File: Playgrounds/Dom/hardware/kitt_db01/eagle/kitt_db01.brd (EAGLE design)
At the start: 50.8 x 31 mm, 13 parts, among them Q1 [MMBF170], U1 ADNS-3080, X1 RESON

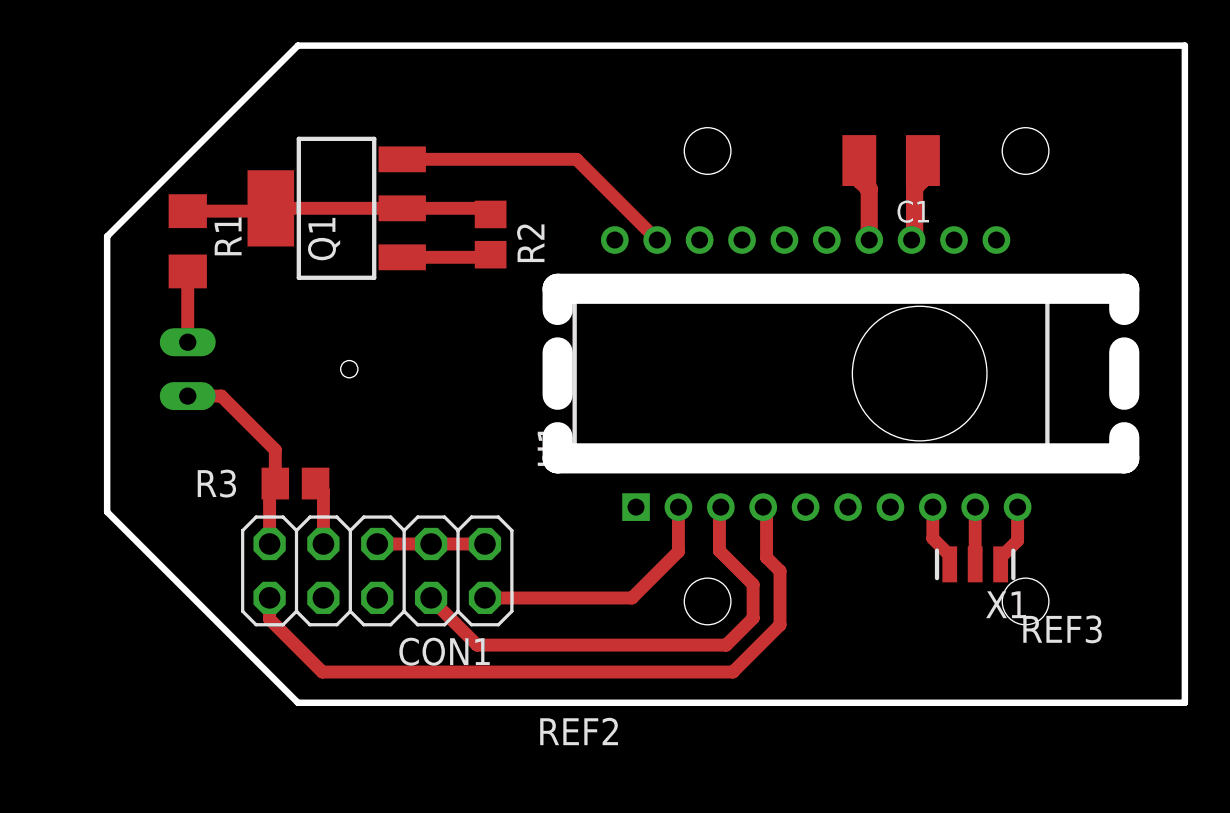
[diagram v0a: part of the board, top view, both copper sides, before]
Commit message: - added poly gnd pour  - cleaned up garbage files
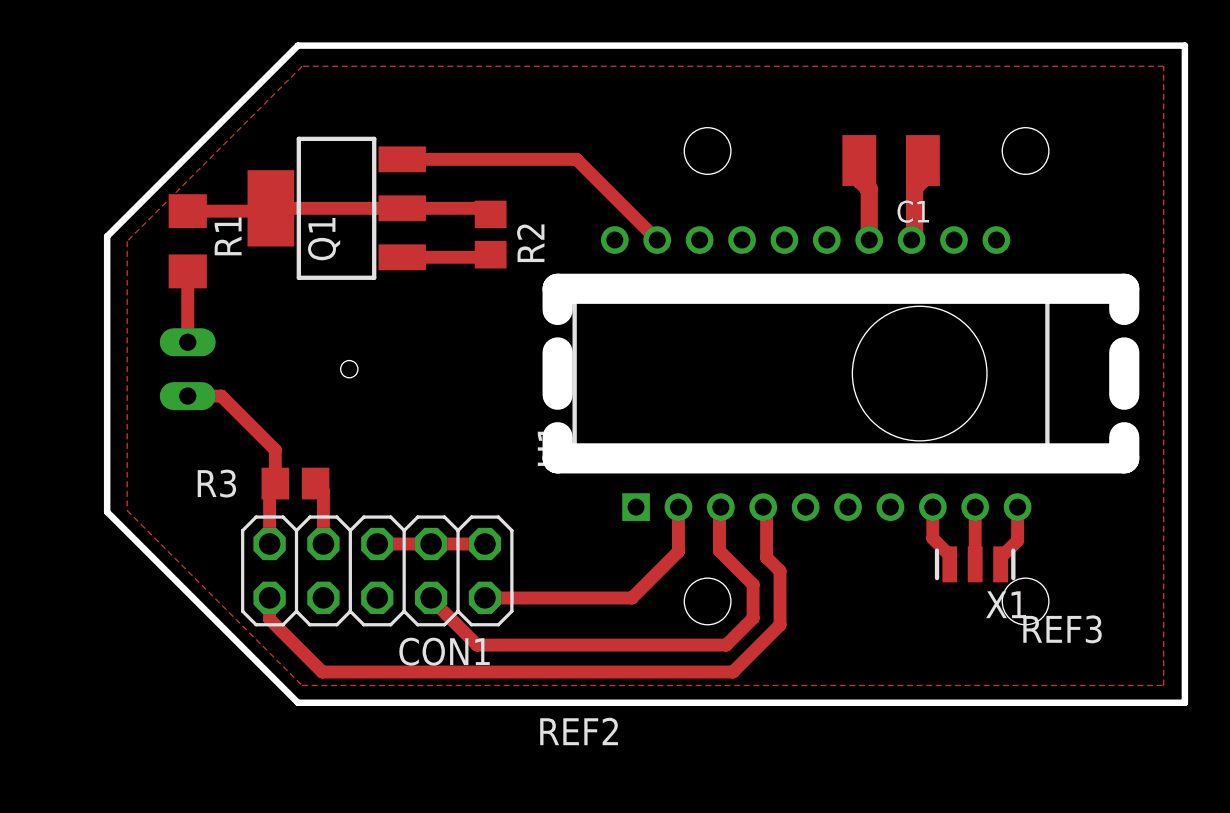
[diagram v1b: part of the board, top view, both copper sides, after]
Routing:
- added copper zone on layer 1, net GND
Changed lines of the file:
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@@
 <setting verticaltext="up"/>
 </settings>
-<grid distance="12.5" unitdist="mil" unit="mil" style="lines" multiple="1" display="yes" altdistance="0.0125" altunitdist="inch" altunit="inch"/>
+<grid distance="25" unitdist="mil" unit="mil" style="lines" multiple="1" display="yes" altdistance="0.0125" altunitdist="inch" altunit="inch"/>
 <layers>
 <layer number="1" name="Top" color="4" fill="1" visible="yes" active="yes"/>
@@
 <wire x1="79.7425" y1="50.49" x2="82.2825" y2="50.49" width="0.6096" layer="1"/>
 <wire x1="82.2825" y1="50.49" x2="84.8225" y2="50.49" width="0.6096" layer="1"/>
-<wire x1="92.949696875" y1="64.829321875" x2="98.949696875" y2="64.829321875" width="0" layer="19" extent="1-1"/>
-<wire x1="84.8225" y1="50.49" x2="92.949696875" y2="64.829321875" width="0" layer="19" extent="1-1"/>
 <wire x1="80.919" y1="68.636" x2="89.14301875" y2="68.636" width="0.6096" layer="1"/>
 <wire x1="89.14301875" y1="68.636" x2="92.949696875" y2="64.829321875" width="0.6096" layer="1"/>
+<polygon width="0.6096" layer="1" isolate="0.4064">
+<vertex x="67.945" y="52.07"/>
+<vertex x="76.2" y="43.815"/>
+<vertex x="116.84" y="43.815"/>
+<vertex x="116.84" y="73.025"/>
+<vertex x="76.2" y="73.025"/>
+<vertex x="67.945" y="64.77"/>
+</polygon>
 </signal>
 <signal name="N$1">
@@
 <contactref element="U1" pad="7"/>
 <contactref element="R3" pad="2"/>
-<wire x1="76.8325" y1="53.34" x2="103.949696875" y2="52.229321875" width="0" layer="19" extent="1-1"/>
 <wire x1="76.8325" y1="53.34" x2="77.2025" y2="52.97" width="0.6096" layer="1"/>
 <wire x1="77.2025" y1="52.97" x2="77.2025" y2="50.49" width="0.6096" layer="1"/>
+<wire x1="77.2025" y1="52.97" x2="103.949696875" y2="52.229321875" width="0" layer="19" extent="1-1"/>
 </signal>
 </signals>

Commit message: added keepout region around milling area
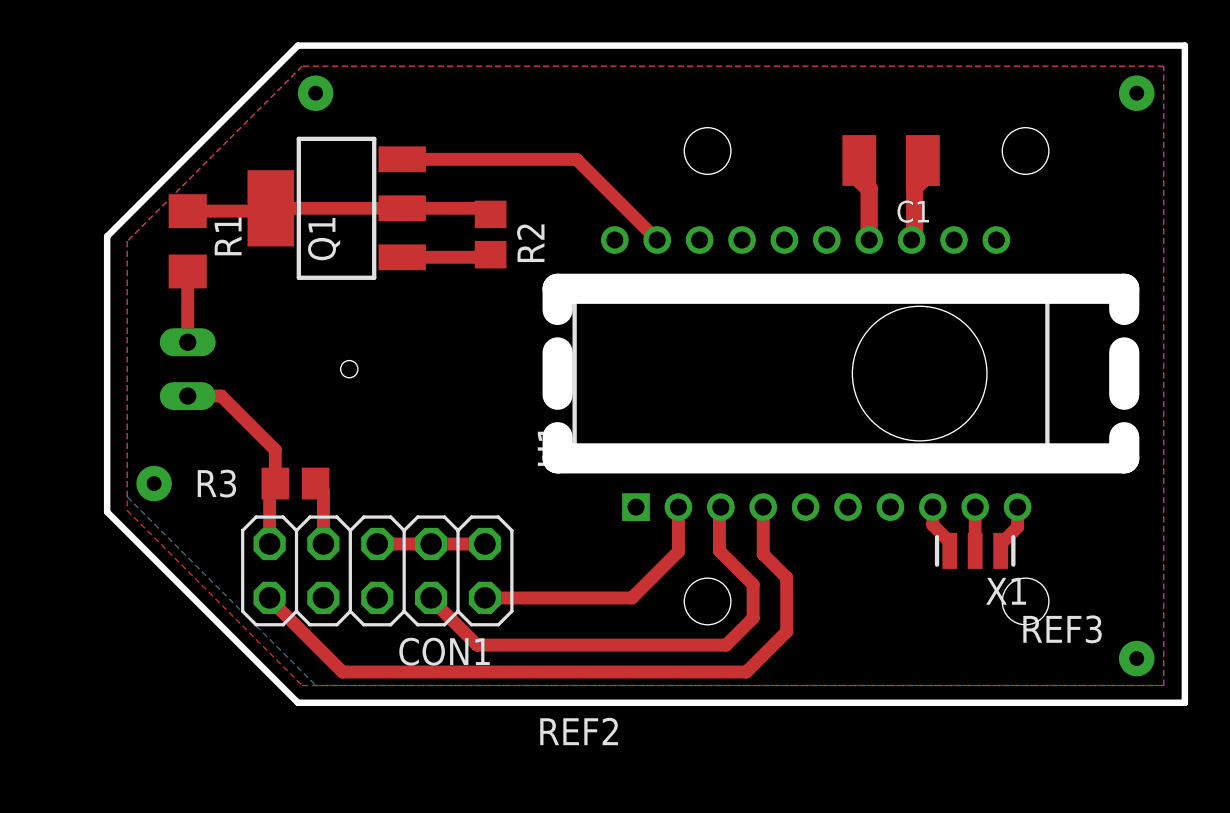
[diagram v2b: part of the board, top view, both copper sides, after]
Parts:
- moved X1 0.63 mm to (107.9, 50.2)
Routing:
- net N$3: track 3.03 -> 2.40 mm
- net N$2: track 3.03 -> 2.40 mm
- net N$1: track 2.70 -> 2.07 mm
- net GND: vias 0 -> 4
- added copper zone on layer 16, net GND
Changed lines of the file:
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@@
 <setting verticaltext="up"/>
 </settings>
-<grid distance="25" unitdist="mil" unit="mil" style="lines" multiple="1" display="yes" altdistance="0.0125" altunitdist="inch" altunit="inch"/>
+<grid distance="25" unitdist="mil" unit="mm" style="lines" multiple="1" display="yes" altdistance="0.0125" altunitdist="inch" altunit="inch"/>
 <layers>
 <layer number="1" name="Top" color="4" fill="1" visible="yes" active="yes"/>
@@
 <wire x1="76" y1="43" x2="117.84" y2="43" width="0.3048" layer="20"/>
 <wire x1="117.84" y1="43" x2="117.84" y2="74" width="0.3048" layer="20"/>
+<polygon width="0.6096" layer="41">
+<vertex x="87.63" y="63.5"/>
+<vertex x="87.63" y="53.34"/>
+<vertex x="116.205" y="53.34"/>
+<vertex x="116.205" y="63.5"/>
+</polygon>
+<polygon width="0.6096" layer="42">
+<vertex x="87.63" y="63.5"/>
+<vertex x="87.63" y="53.34"/>
+<vertex x="116.205" y="53.34"/>
+<vertex x="116.205" y="63.5"/>
+</polygon>
 </plain>
 <attributes>
@@
 <element name="REF3" library="scaleauto" package="SC-8000-C" value="SC-8000-C" x="126.575696875" y="58.529321875"/>
 <element name="U1" library="Ai_IC" package="ADNS-3080" value="ADNS-3080" x="100.075696875" y="58.529321875"/>
-<element name="X1" library="Ai_Passives" package="RESON-SMD" value="RESON" x="107.948696875" y="49.529321875" rot="R180"/>
+<element name="X1" library="Ai_Passives" package="RESON-SMD" value="RESON" x="107.948696875" y="50.164321875" rot="R180"/>
 <element name="U$1" library="frames" package="A3L-LOC" value="" x="-113.3475" y="-77.1525"/>
 <element name="CON1" library="pinhead" package="2X05" value="" x="79.7425" y="49.22" smashed="yes">
@@
 <vertex x="67.945" y="64.77"/>
 </polygon>
+<via x="69.215" y="53.34" extent="1-16" drill="0.7" diameter="1.6764"/>
+<polygon width="0.6096" layer="16" isolate="0.4064">
+<vertex x="67.945" y="64.77"/>
+<vertex x="67.945" y="52.705"/>
+<vertex x="76.835" y="43.815"/>
+<vertex x="116.84" y="43.815"/>
+<vertex x="116.84" y="73.025"/>
+<vertex x="76.2" y="73.025"/>
+</polygon>
+<via x="76.835" y="71.755" extent="1-16" drill="0.7" diameter="1.6764"/>
+<via x="115.57" y="71.755" extent="1-16" drill="0.7" diameter="1.6764"/>
+<via x="115.57" y="45.085" extent="1-16" drill="0.7" diameter="1.6764"/>
 </signal>
 <signal name="N$1">
 <contactref element="U1" pad="9"/>
 <contactref element="X1" pad="2"/>
-<wire x1="107.948696875" y1="49.529321875" x2="107.949696875" y2="49.530321875" width="0.6096" layer="1"/>
-<wire x1="107.949696875" y1="49.530321875" x2="107.949696875" y2="52.229321875" width="0.6096" layer="1"/>
+<wire x1="107.948696875" y1="50.164321875" x2="107.949696875" y2="50.165321875" width="0.6096" layer="1"/>
+<wire x1="107.949696875" y1="50.165321875" x2="107.949696875" y2="52.229321875" width="0.6096" layer="1"/>
 </signal>
 <signal name="N$2">
 <contactref element="X1" pad="3"/>
 <contactref element="U1" pad="8"/>
-<wire x1="105.949696875" y1="52.229321875" x2="105.949696875" y2="50.750521875" width="0.6096" layer="1"/>
-<wire x1="105.949696875" y1="50.750521875" x2="106.748696875" y2="49.951521875" width="0.6096" layer="1"/>
-<wire x1="106.748696875" y1="49.951521875" x2="106.748696875" y2="49.529321875" width="0.6096" layer="1"/>
+<wire x1="105.949696875" y1="52.229321875" x2="105.949696875" y2="51.385521875" width="0.6096" layer="1"/>
+<wire x1="105.949696875" y1="51.385521875" x2="106.748696875" y2="50.586521875" width="0.6096" layer="1"/>
+<wire x1="106.748696875" y1="50.586521875" x2="106.748696875" y2="50.164321875" width="0.6096" layer="1"/>
 </signal>
 <signal name="N$3">
 <contactref element="X1" pad="1"/>
 <contactref element="U1" pad="10"/>
-<wire x1="109.949696875" y1="52.229321875" x2="109.949696875" y2="50.648321875" width="0.6096" layer="1"/>
-<wire x1="109.949696875" y1="50.648321875" x2="109.148696875" y2="49.847321875" width="0.6096" layer="1"/>
-<wire x1="109.148696875" y1="49.847321875" x2="109.148696875" y2="49.529321875" width="0.6096" layer="1"/>
+<wire x1="109.949696875" y1="52.229321875" x2="109.949696875" y2="51.283321875" width="0.6096" layer="1"/>
+<wire x1="109.949696875" y1="51.283321875" x2="109.148696875" y2="50.482321875" width="0.6096" layer="1"/>
+<wire x1="109.148696875" y1="50.482321875" x2="109.148696875" y2="50.164321875" width="0.6096" layer="1"/>
 </signal>
 <signal name="+3V3">
@@
 <contactref element="CON1" pad="1"/>
 <contactref element="U1" pad="4"/>
-<wire x1="97.949696875" y1="52.229321875" x2="98.1075" y2="52.07151875" width="0.6096" layer="1"/>
-<wire x1="98.1075" y1="52.07151875" x2="98.1075" y2="49.8475" width="0.6096" layer="1"/>
-<wire x1="98.1075" y1="49.8475" x2="98.7425" y2="49.2125" width="0.6096" layer="1"/>
-<wire x1="98.7425" y1="49.2125" x2="98.7425" y2="46.6725" width="0.6096" layer="1"/>
-<wire x1="98.7425" y1="46.6725" x2="96.52" y2="44.45" width="0.6096" layer="1"/>
-<wire x1="96.52" y1="44.45" x2="77.1525" y2="44.45" width="0.6096" layer="1"/>
-<wire x1="77.1525" y1="44.45" x2="74.6625" y2="46.94" width="0.6096" layer="1"/>
-<wire x1="74.6625" y1="46.94" x2="74.6625" y2="47.95" width="0.6096" layer="1"/>
+<wire x1="74.6625" y1="47.95" x2="74.6625" y2="47.8925" width="0.6096" layer="1"/>
+<wire x1="74.6625" y1="47.8925" x2="78.105" y2="44.45" width="0.6096" layer="1"/>
+<wire x1="78.105" y1="44.45" x2="97.155" y2="44.45" width="0.6096" layer="1"/>
+<wire x1="97.155" y1="44.45" x2="99.06" y2="46.355" width="0.6096" layer="1"/>
+<wire x1="99.06" y1="46.355" x2="99.06" y2="48.895" width="0.6096" layer="1"/>
+<wire x1="99.06" y1="48.895" x2="97.949696875" y2="50.005303125" width="0.6096" layer="1"/>
+<wire x1="97.949696875" y1="50.005303125" x2="97.949696875" y2="52.229321875" width="0.6096" layer="1"/>
 </signal>
 <signal name="RST">

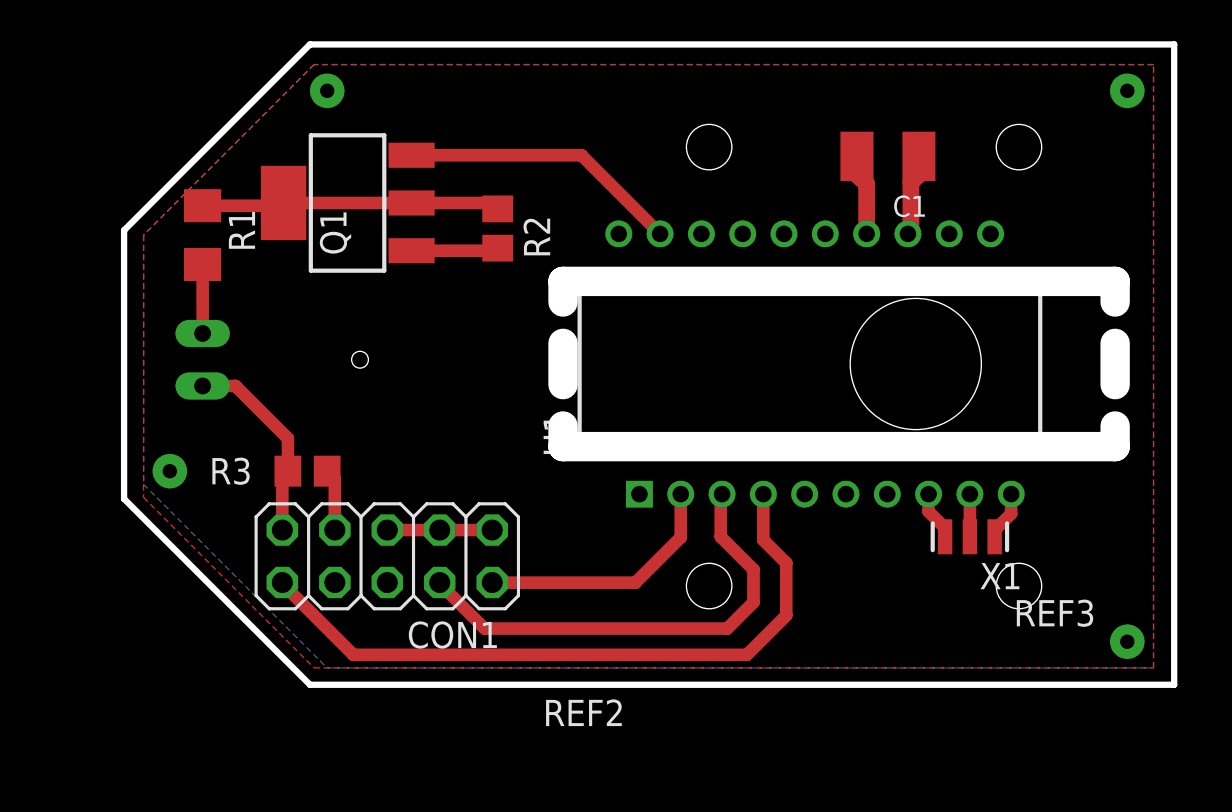
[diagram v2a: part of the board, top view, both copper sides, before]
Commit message: rough route and placement completed
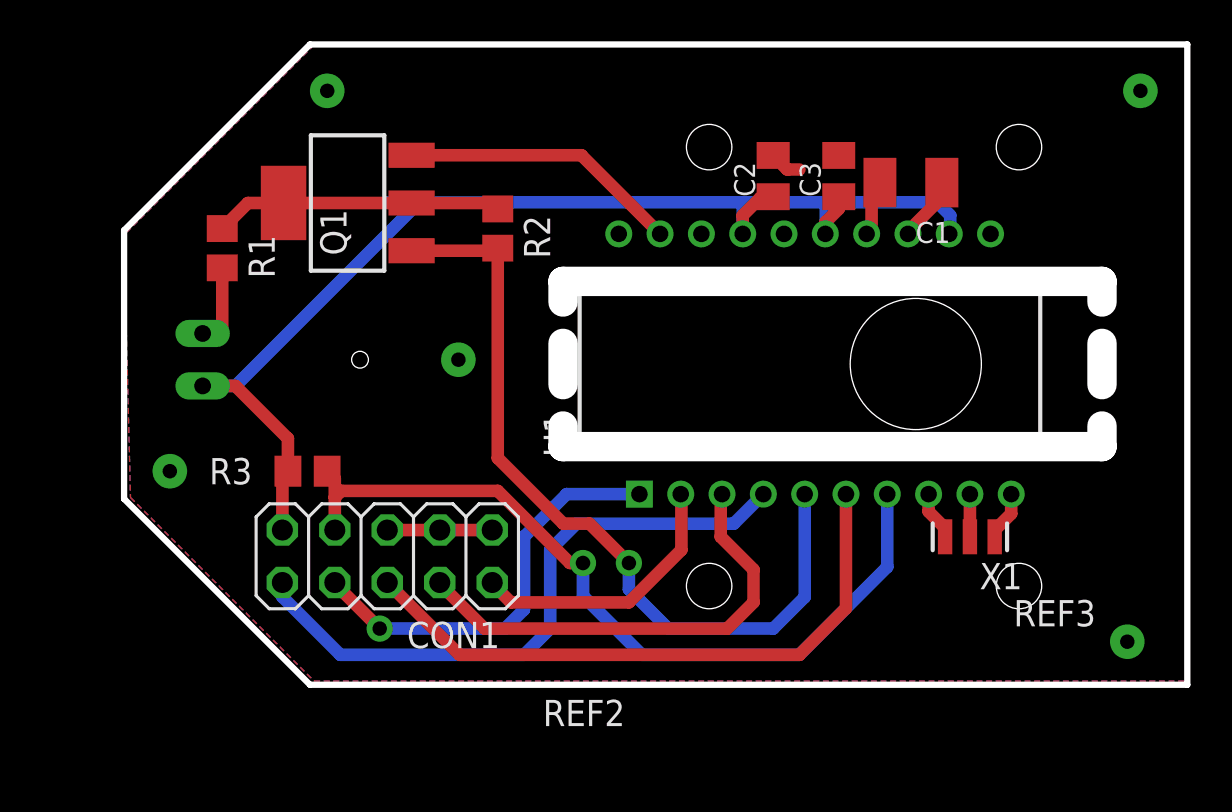
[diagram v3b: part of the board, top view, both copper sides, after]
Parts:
- added C2, C3: 100nF, rcl:C0805K
- R1: device rcl:R1206 -> rcl:R0805
- moved C1 1.69 mm to (105.1, 67.3)
- moved R1 1.14 mm to (71.8, 64.1)
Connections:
- net +3V3: now also C2.1, C3.1
- net GND: now also C2.2, C3.2
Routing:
- net +3V3: track 9.73 -> 60.3 mm
- net !PD: track 3.00 -> 39.4 mm, vias 0 -> 1
- net N$4: track 4.22 -> 39.0 mm, vias 0 -> 1
- net RST: track 0.00 -> 30.1 mm
- net !CS: track 0.00 -> 20.5 mm, vias 0 -> 1
- net MOSI: track 33.0 -> 30.8 mm
- net GND: track 18.7 -> 20.3 mm, vias 4 -> 5
- net MISO: track 12.1 -> 13.4 mm
- net N$6: track 3.94 -> 2.75 mm
- net N$5: track 3.97 -> 3.08 mm
- net N$8: track 3.34 -> 4.13 mm
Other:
- board size 50.8 x 31 mm -> 51.5 x 31 mm

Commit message: Board and Library Updates  - kitt.con.lbr: connectors and connector references    -> DB01 Odometry Board Connector + board outline    -> Arduino Uno shield pins + (pin) overlay for ghostcar  - kitt.ic.lbr: added battery charger component from prev. board
 - mb01.*: motherboard for scaleauto
   -> added board connectors
   -> extended board size and corrected mounting holes
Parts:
- added R4: [PPR], rcl:R0805
- moved R3 0.63 mm to (75.9, 54.0)
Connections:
- net !PD: now also R4.1
- net GND: now also R4.2
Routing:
- net !PD: track 39.4 -> 42.1 mm
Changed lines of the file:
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@@
 <element name="R2" library="rcl" package="R0805" value="[0R]" x="85.09" y="65.0875" rot="R270"/>
 <element name="R1" library="rcl" package="R0805" value="180R" x="71.755" y="64.135" rot="R270"/>
-<element name="R3" library="rcl" package="R0805" value="[PPR]" x="75.8825" y="53.34" smashed="yes">
-<attribute name="NAME" x="71.12" y="52.705" size="1.27" layer="25"/>
-<attribute name="VALUE" x="78.4225" y="53.0225" size="1.27" layer="27"/>
+<element name="R3" library="rcl" package="R0805" value="[PPR]" x="75.8825" y="53.975" smashed="yes">
+<attribute name="NAME" x="71.12" y="53.34" size="1.27" layer="25"/>
+<attribute name="VALUE" x="78.4225" y="53.6575" size="1.27" layer="27"/>
 </element>
 <element name="C2" library="rcl" package="C0805K" value="100nF" x="98.425" y="67.6275" rot="R90"/>
 <element name="C3" library="rcl" package="C0805K" value="100nF" x="101.6" y="67.6275" rot="R90"/>
+<element name="R4" library="rcl" package="R0805" value="[PPR]" x="80.01" y="53.975"/>
 </elements>
 <signals>
@@
 <wire x1="98.425" y1="68.6275" x2="99.1075" y2="67.945" width="0.6096" layer="1"/>
 <wire x1="99.1075" y1="67.945" x2="99.695" y2="67.945" width="0.6096" layer="1"/>
+<contactref element="R4" pad="2"/>
 </signal>
 <signal name="N$1">
@@
 <contactref element="U1" pad="17"/>
 <contactref element="R3" pad="1"/>
-<wire x1="74.6625" y1="50.49" x2="74.6625" y2="53.07" width="0.6096" layer="1"/>
-<wire x1="74.6625" y1="53.07" x2="74.9325" y2="53.34" width="0.6096" layer="1"/>
-<wire x1="74.9325" y1="53.34" x2="74.9325" y2="54.925" width="0.6096" layer="1"/>
+<wire x1="74.6625" y1="50.49" x2="74.6625" y2="53.3875" width="0.6096" layer="1"/>
+<wire x1="74.6625" y1="53.3875" x2="74.9325" y2="53.975" width="0.6096" layer="1"/>
+<wire x1="74.9325" y1="53.975" x2="74.9325" y2="54.925" width="0.6096" layer="1"/>
 <wire x1="74.9325" y1="54.925" x2="72.39" y2="57.4675" width="0.6096" layer="1"/>
 <wire x1="72.39" y1="57.4675" x2="70.8025" y2="57.4675" width="0.6096" layer="1"/>
@@
 <contactref element="U1" pad="7"/>
 <contactref element="R3" pad="2"/>
-<wire x1="76.8325" y1="53.34" x2="77.2025" y2="52.97" width="0.6096" layer="1"/>
-<wire x1="77.2025" y1="52.97" x2="77.2025" y2="52.07" width="0.6096" layer="1"/>
-<wire x1="77.2025" y1="52.07" x2="77.2025" y2="50.49" width="0.6096" layer="1"/>
+<wire x1="76.8325" y1="53.975" x2="77.2025" y2="53.605" width="0.6096" layer="1"/>
+<wire x1="77.2025" y1="53.605" x2="77.2025" y2="52.3875" width="0.6096" layer="1"/>
+<wire x1="77.2025" y1="52.3875" x2="77.2025" y2="50.49" width="0.6096" layer="1"/>
 <wire x1="103.949696875" y1="52.229321875" x2="103.949696875" y2="48.704696875" width="0.6096" layer="16"/>
 <wire x1="103.949696875" y1="48.704696875" x2="99.695" y2="44.45" width="0.6096" layer="16"/>
@@
 <wire x1="89.2175" y1="48.895" x2="88.5825" y2="48.895" width="0.6096" layer="1"/>
 <wire x1="88.5825" y1="48.895" x2="85.09" y2="52.3875" width="0.6096" layer="1"/>
-<wire x1="85.09" y1="52.3875" x2="77.52" y2="52.3875" width="0.6096" layer="1"/>
-<wire x1="77.52" y1="52.3875" x2="77.2025" y2="52.07" width="0.6096" layer="1"/>
+<wire x1="85.09" y1="52.3875" x2="77.2025" y2="52.3875" width="0.6096" layer="1"/>
+<contactref element="R4" pad="1"/>
+<wire x1="79.06" y1="53.975" x2="76.8325" y2="53.975" width="0.6096" layer="1"/>
 </signal>
 </signals>
